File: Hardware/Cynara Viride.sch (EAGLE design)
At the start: 171 parts, among them Q1 TXC-7B, Q2 TXC-7WNEO, SW1 430181038816, SW2 , T1 PDTC143, T2 PDTC143, T3 PDTC143, T4 PDTC143, T5 PDTC143, U1 TM4C129EN, U2 MCP1826S 3V3, U3 LM4132 3V3, U4 XC6SLX9-3TQG, U5 M25P16-SO8, U6 MCP1826S 1V2, U7 , X1 EDGE 50p, X11 SOCK2X17, X12 SOCK2X17, X13 SOCK2X17, X2 EDGE 50p, X23 debug xilinx, X24 debug 10p, X3 EDGE 50p, X4 EDGE 50p, X5 MicroMatch 24, X6 USB C socket, X7 SOCK2X17, X8 RJ45-LAN-10/100

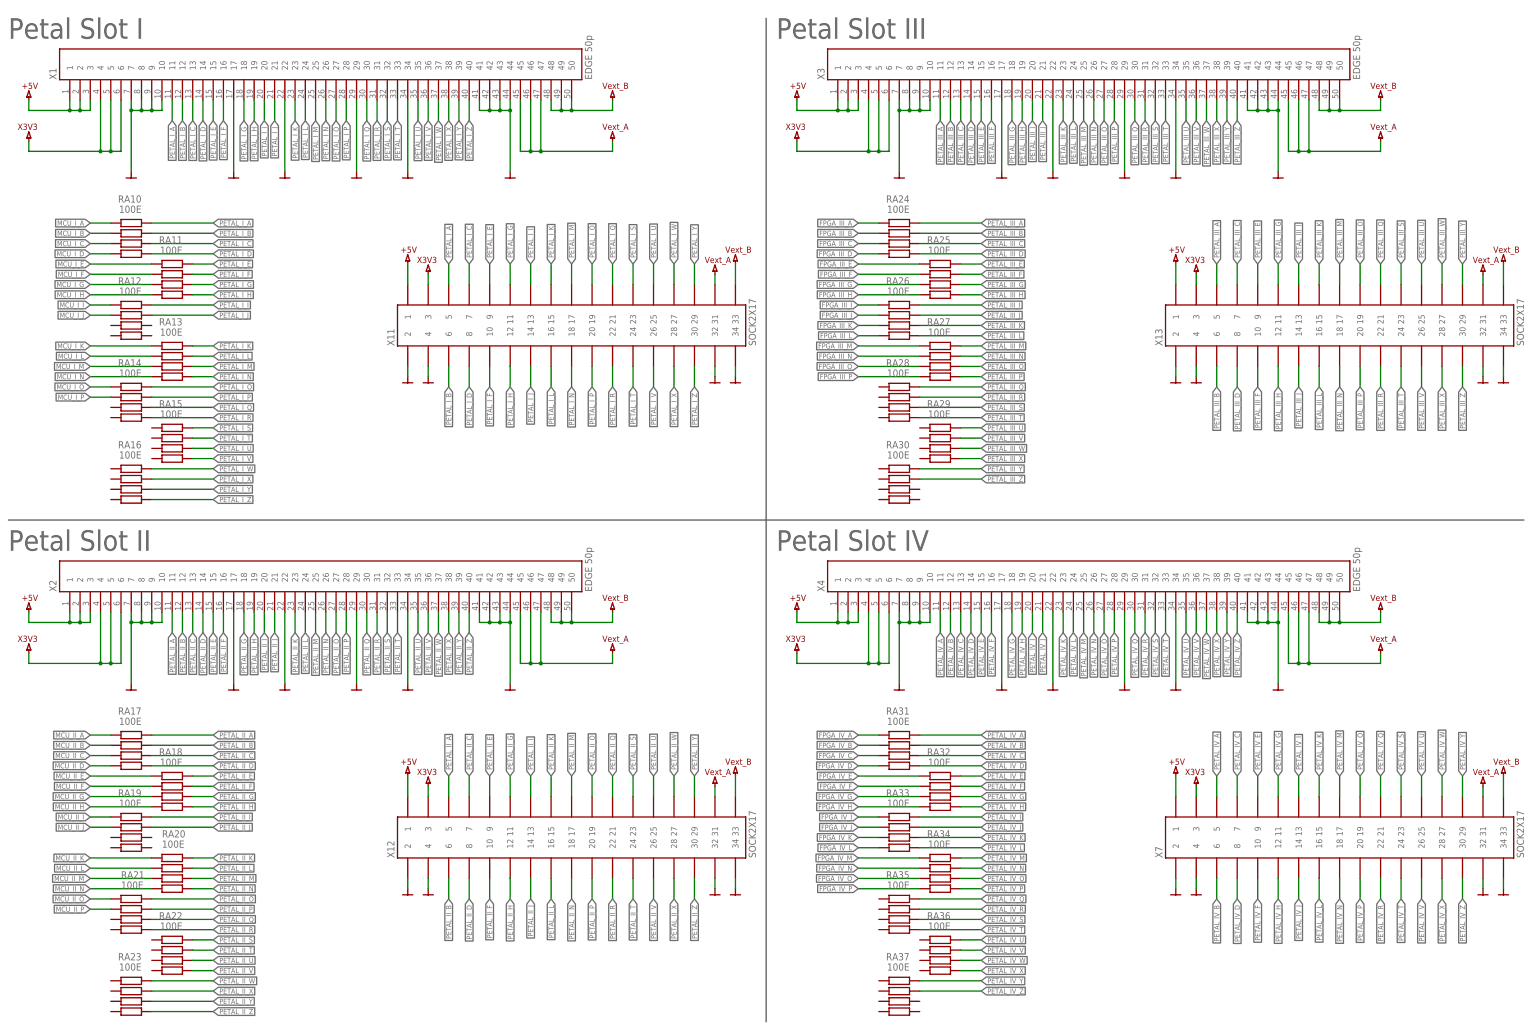
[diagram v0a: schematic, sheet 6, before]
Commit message: [WIP] Moved FPGA and MCU to make space for Ethernet and USB.
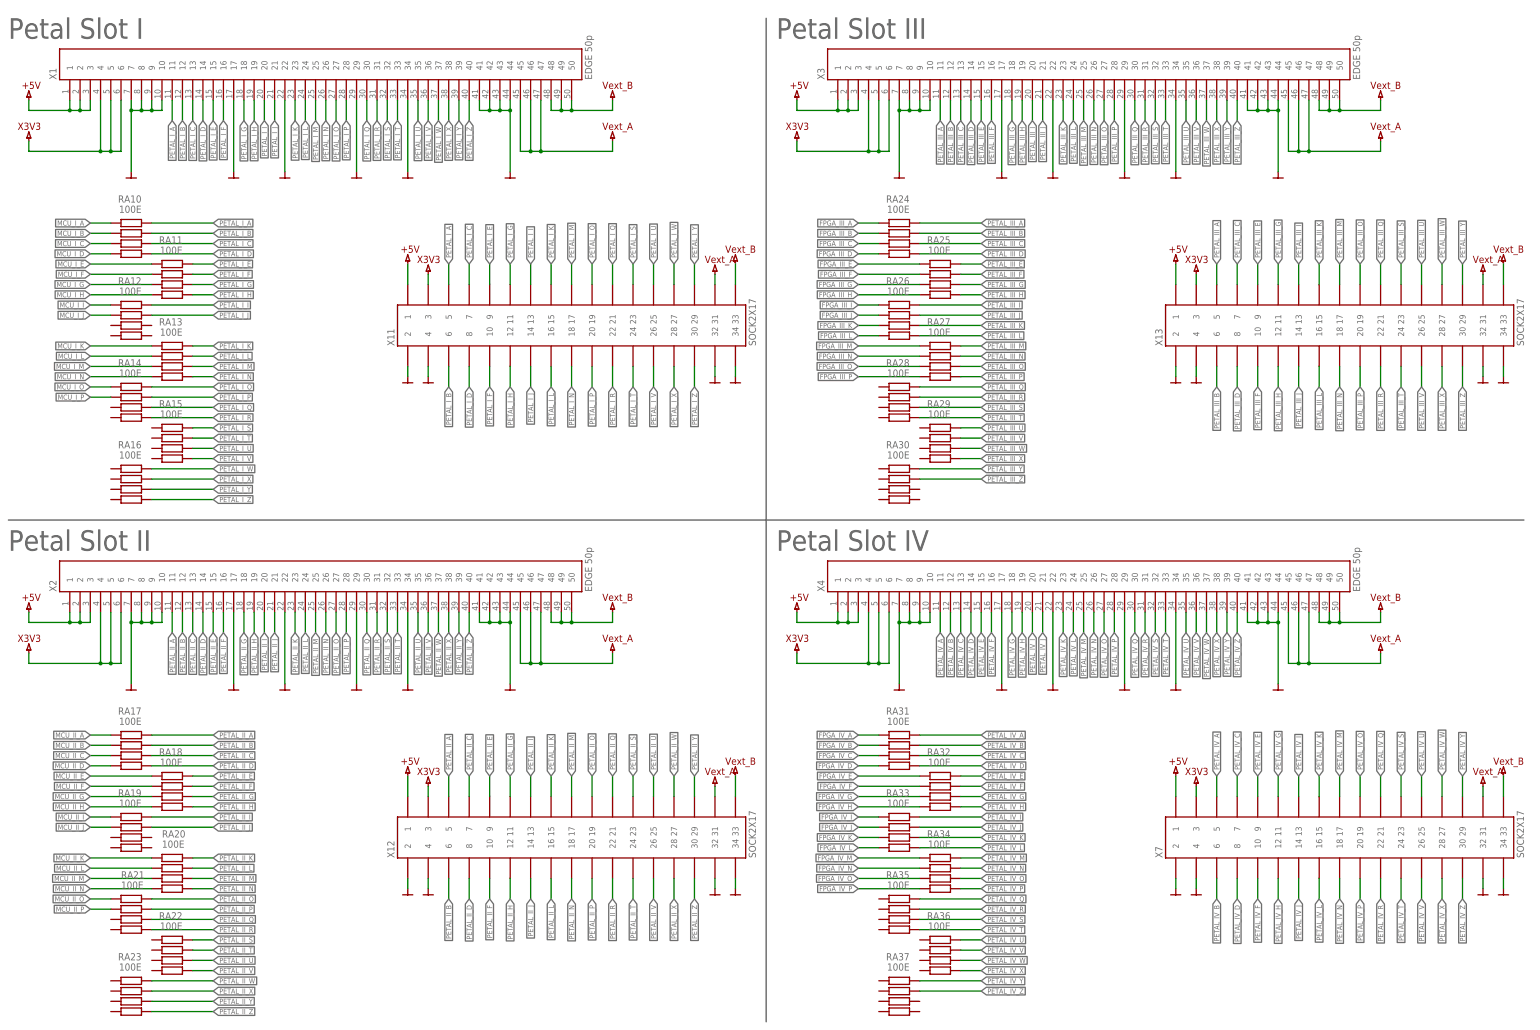
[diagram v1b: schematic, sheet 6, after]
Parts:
- removed DISP1: (no value), Cynara-Misc:ADAFRUIT_OLED
- removed R29: 900k, Cynara-Passives:R-EU_R0603
- removed U7: (no value), Cynara-IntegratedCircuits:TUSB320
- X6: value USB C socket -> (none); device Cynara-Connectors:USB-C-RECEPTICAL-RA -> Cynara-Connectors:USB2.0-TYPE-B
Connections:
- removed net CC1: U7.CC1, X6.CC1
- removed net CC2: U7.CC2, X6.CC2
- removed net N$18: R29.1, U7.VBUS_DET
- net +3.3V: now also U5A.!HOLD; no longer DISP1.VIN, U5A.HOLD, U7.VDD
- net 5V_USB: no longer R29.2
- net D_N: no longer X6.D1-, X6.D2-
- net D_P: no longer X6.D1+, X6.D2+
- net GND: now also X6.GND; no longer DISP1.GND, U7.!EN, U7.GND, U7.PORT, X6.GND@1, X6.GND@2, X6.GND@3, X6.GND@4
- net OLED_CS: no longer DISP1.!CS
- net OLED_DC: no longer DISP1.!DC
- net OLED_MOSI: no longer DISP1.MOSI
- net OLED_RST: no longer DISP1.!RST
- net OLED_SCLK: no longer DISP1.SCLK
- net PJ1X: now also U5A.!WP; no longer U5A.WP
- net SSI0FSS: now also U5A.!CS; no longer U5A.CS
- net USB_DETECT1: no longer U7.OUT1
- net USB_DETECT2: no longer U7.OUT2
- net VBUS: no longer X6.VBUS@1, X6.VBUS@2, X6.VBUS@3, X6.VBUS@4

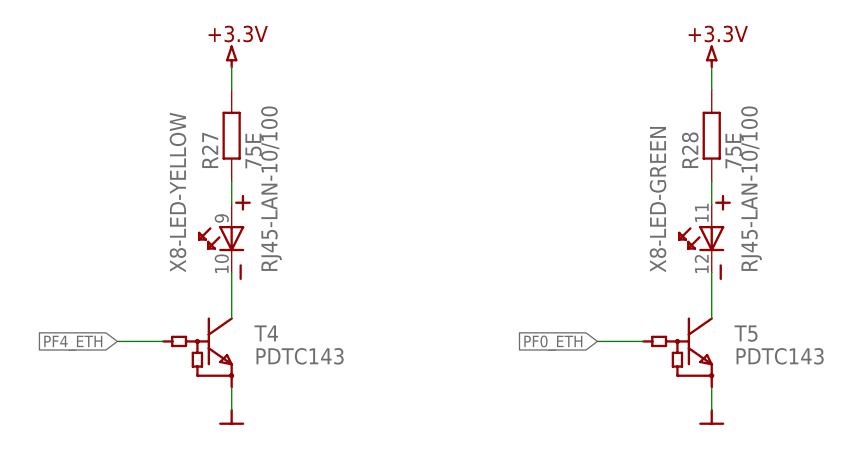
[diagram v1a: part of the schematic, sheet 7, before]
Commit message: Layout for Ethernet and USB 2.0. Fixed problem with VREFA+ being too close to EPI clock signal.
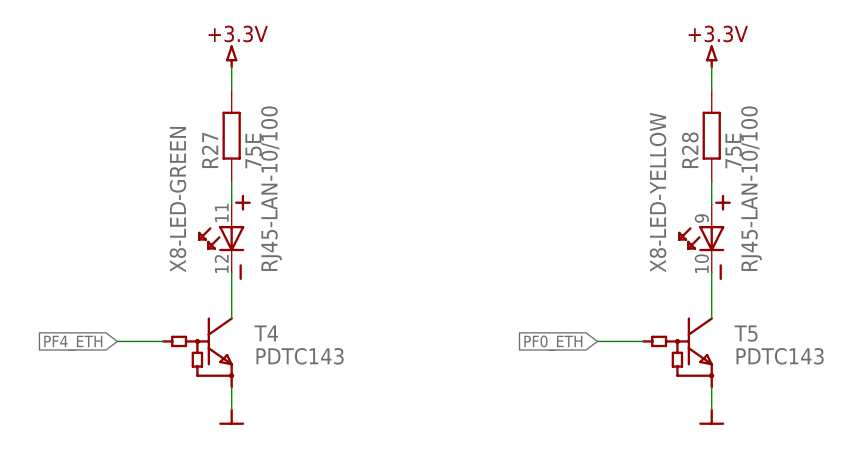
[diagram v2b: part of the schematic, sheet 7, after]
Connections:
- removed net N$22: T5.C, X8-LED-GREEN.K
- removed net N$23: R27.1, X8-LED-YELLOW.A
- removed net N$24: R28.1, X8-LED-GREEN.A
- new net N$14: T4.C, X8-LED-GREEN.K
- new net N$18: R28.1, X8-LED-YELLOW.A
- new net N$6: R27.1, X8-LED-GREEN.A
- net D_N: now also X6.D_N
- net D_P: now also X6.D_P
- net N$21: now also T5.C; no longer T4.C
- net VBUS: now also X6.VCC
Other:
- moved on the sheet: X8-LED-GREEN, X8-LED-YELLOW
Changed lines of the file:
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@@
 <setting verticaltext="up"/>
 </settings>
-<grid distance="0.1" unitdist="inch" unit="inch" style="lines" multiple="1" display="no" altdistance="0.01" altunitdist="inch" altunit="inch"/>
+<grid distance="0.1" unitdist="inch" unit="inch" style="lines" multiple="1" display="yes" altdistance="0.01" altunitdist="inch" altunit="inch"/>
 <layers>
 <layer number="1" name="Top" color="4" fill="1" visible="no" active="no"/>
@@
 <instance part="U$29" gate=" " x="307.34" y="233.68"/>
 <instance part="X8" gate="-RJ45-LAN" x="167.64" y="200.66"/>
-<instance part="X8" gate="-LED-YELLOW" x="254" y="210.82" rot="R90"/>
-<instance part="X8" gate="-LED-GREEN" x="307.34" y="210.82" rot="R90"/>
+<instance part="X8" gate="-LED-YELLOW" x="307.34" y="210.82" rot="R90"/>
+<instance part="X8" gate="-LED-GREEN" x="254" y="210.82" rot="R90"/>
 <instance part="X8" gate="-SHIELD" x="208.28" y="170.18"/>
 <instance part="R27" gate="G$1" x="254" y="223.52" rot="R90"/>
@@
 <wire x1="203.2" y1="78.74" x2="198.12" y2="78.74" width="0.1524" layer="91"/>
 <label x="198.12" y="78.74" size="1.27" layer="95" rot="R180" xref="yes"/>
+<pinref part="X6" gate="X1" pin="VCC"/>
 </segment>
 </net>
@@
 <wire x1="203.2" y1="76.2" x2="198.12" y2="76.2" width="0.1524" layer="91"/>
 <label x="198.12" y="76.2" size="1.27" layer="95" rot="R180" xref="yes"/>
+<pinref part="X6" gate="X1" pin="D_N"/>
 </segment>
 </net>
@@
 <wire x1="203.2" y1="73.66" x2="198.12" y2="73.66" width="0.1524" layer="91"/>
 <label x="198.12" y="73.66" size="1.27" layer="95" rot="R180" xref="yes"/>
+<pinref part="X6" gate="X1" pin="D_P"/>
 </segment>
 </net>
@@
 </segment>
 </net>
-<net name="N$21" class="0">
+<net name="5V_USB" class="0">
 <segment>
-<pinref part="T4" gate="G$1" pin="C"/>
-<wire x1="254" y1="208.28" x2="254" y2="203.2" width="0.1524" layer="91"/>
-<pinref part="X8" gate="-LED-YELLOW" pin="K"/>
+<pinref part="L4" gate="G$1" pin="E"/>
+<wire x1="101.6" y1="96.52" x2="86.36" y2="96.52" width="0.1524" layer="91"/>
+<label x="86.36" y="96.52" size="1.27" layer="95" rot="R180" xref="yes"/>
 </segment>
 </net>
-<net name="N$22" class="0">
+<net name="N$6" class="0">
 <segment>
-<pinref part="T5" gate="G$1" pin="C"/>
-<wire x1="307.34" y1="208.28" x2="307.34" y2="203.2" width="0.1524" layer="91"/>
-<pinref part="X8" gate="-LED-GREEN" pin="K"/>
+<pinref part="R27" gate="G$1" pin="1"/>
+<pinref part="X8" gate="-LED-GREEN" pin="A"/>
+<wire x1="254" y1="218.44" x2="254" y2="215.9" width="0.1524" layer="91"/>
 </segment>
 </net>
-<net name="N$23" class="0">
+<net name="N$14" class="0">
 <segment>
-<pinref part="R27" gate="G$1" pin="1"/>
-<pinref part="X8" gate="-LED-YELLOW" pin="A"/>
-<wire x1="254" y1="218.44" x2="254" y2="215.9" width="0.1524" layer="91"/>
+<pinref part="X8" gate="-LED-GREEN" pin="K"/>
+<pinref part="T4" gate="G$1" pin="C"/>
+<wire x1="254" y1="208.28" x2="254" y2="203.2" width="0.1524" layer="91"/>
 </segment>
 </net>
-<net name="N$24" class="0">
+<net name="N$18" class="0">
 <segment>
 <pinref part="R28" gate="G$1" pin="1"/>
-<pinref part="X8" gate="-LED-GREEN" pin="A"/>
+<pinref part="X8" gate="-LED-YELLOW" pin="A"/>
 <wire x1="307.34" y1="218.44" x2="307.34" y2="215.9" width="0.1524" layer="91"/>
 </segment>
 </net>
-<net name="5V_USB" class="0">
+<net name="N$21" class="0">
 <segment>
-<pinref part="L4" gate="G$1" pin="E"/>
-<wire x1="101.6" y1="96.52" x2="86.36" y2="96.52" width="0.1524" layer="91"/>
-<label x="86.36" y="96.52" size="1.27" layer="95" rot="R180" xref="yes"/>
+<pinref part="X8" gate="-LED-YELLOW" pin="K"/>
+<pinref part="T5" gate="G$1" pin="C"/>
+<wire x1="307.34" y1="208.28" x2="307.34" y2="203.2" width="0.1524" layer="91"/>
 </segment>
 </net>

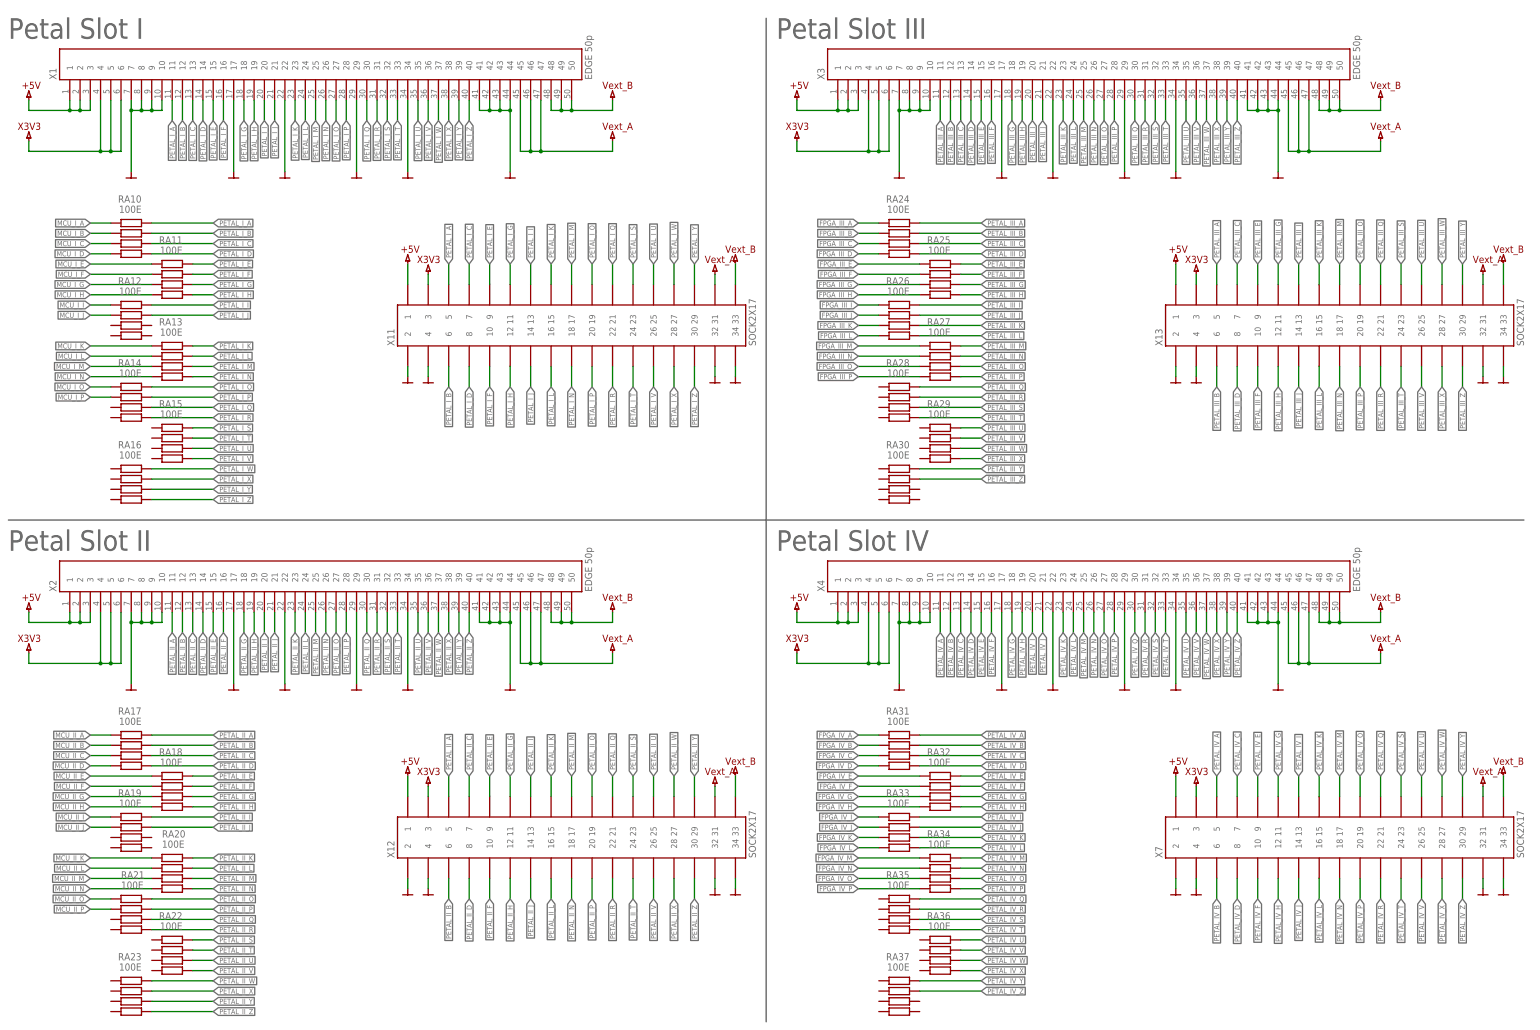
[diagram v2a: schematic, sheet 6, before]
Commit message: Added proposal for power routing to the Petals.
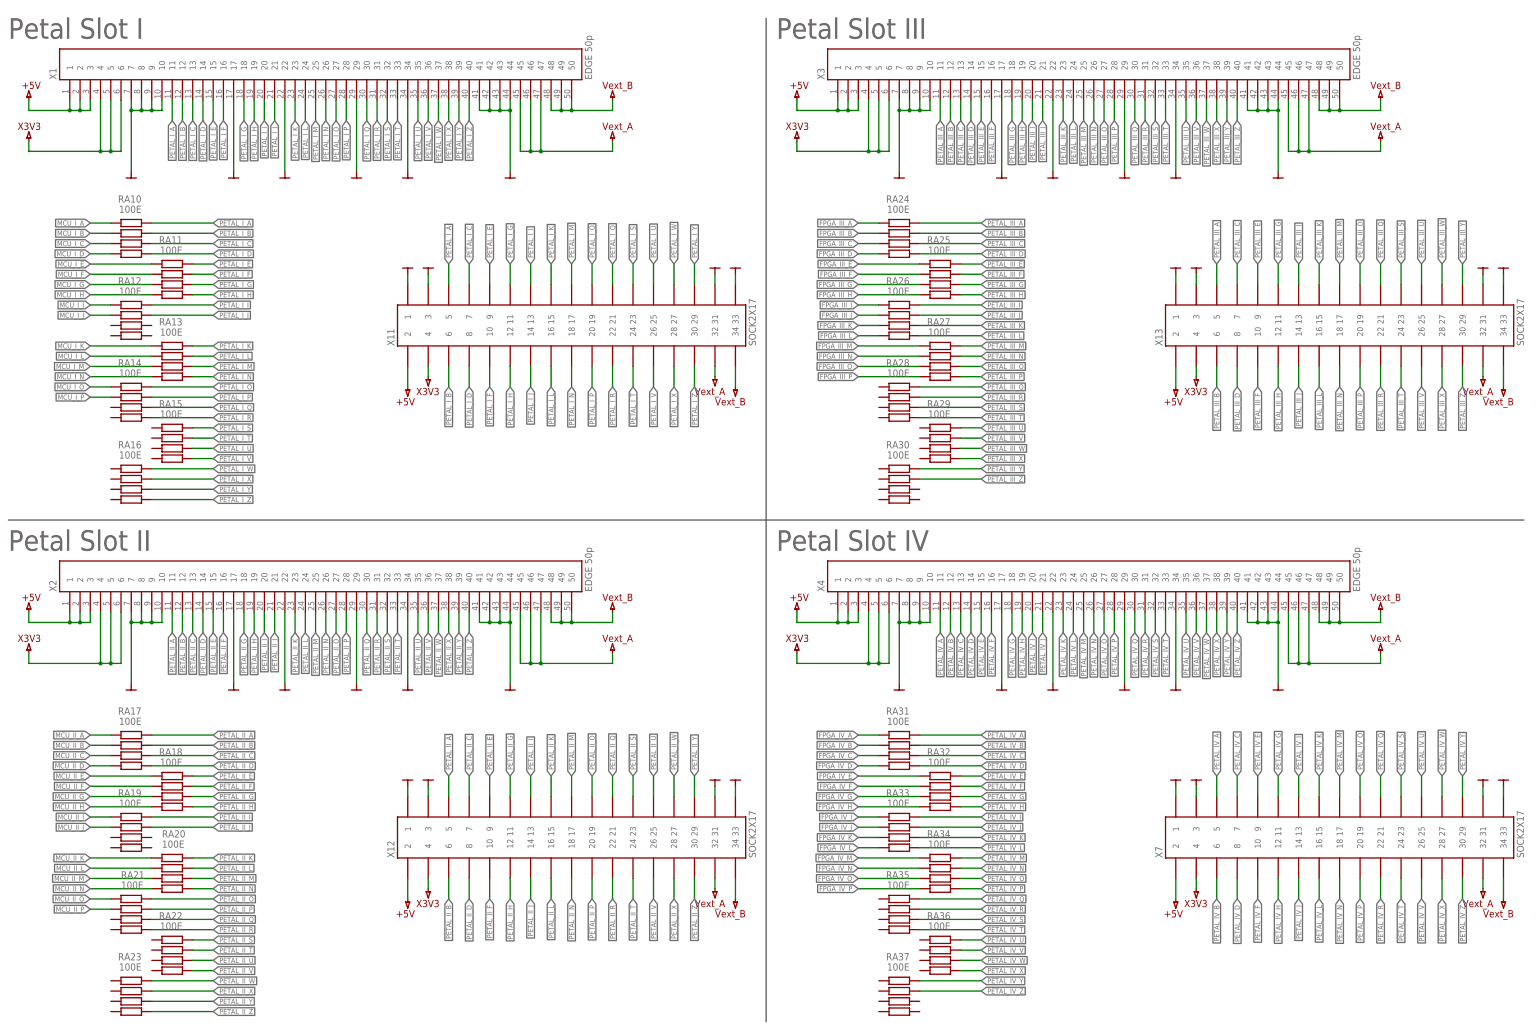
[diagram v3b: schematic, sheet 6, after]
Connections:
- net +5V: now also X11.2, X12.2, X13.2, X7.2; no longer X11.1, X12.1, X13.1, X7.1
- net GND: now also X11.1, X11.3, X11.31, X11.33, X12.1, X12.3, X12.31, X12.33, X13.1, X13.3, X13.31, X13.33, X7.1, X7.3, X7.31, X7.33; no longer X11.2, X11.32, X11.34, X11.4, X12.2, X12.32, X12.34, X12.4, X13.2, X13.32, X13.34, X13.4, X7.2, X7.32, X7.34, X7.4
- net VEXT_A: now also X11.32, X12.32, X13.32, X7.32; no longer X11.31, X12.31, X13.31, X7.31
- net VEXT_B: now also X11.34, X12.34, X13.34, X7.34; no longer X11.33, X12.33, X13.33, X7.33
- net X3V3: now also X11.4, X12.4, X13.4, X7.4; no longer X11.3, X12.3, X13.3, X7.3
